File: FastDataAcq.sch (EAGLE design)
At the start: 225 parts, among them J1 MICRO-FIT_3.0_2POS_RA_SMD, J2 USB_MICROAB_SMT, U1 ADC08D500, U10 TMP421, U11 DAC101C081, U12 ADCMP553BRMZ, U13 XCFXXS04, U14 FT230XQ, U2 XC6SLX9-3TQG144C, U3 LTC2955-1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

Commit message: Minor
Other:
- note added: "1"
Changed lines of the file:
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@@
 <text x="239.522" y="157.48" size="1.778" layer="96">Green</text>
 <text x="249.682" y="157.48" size="1.778" layer="96">Red</text>
+<text x="419.1" y="7.62" size="1.778" layer="91">1</text>
 </plain>
 <instances>

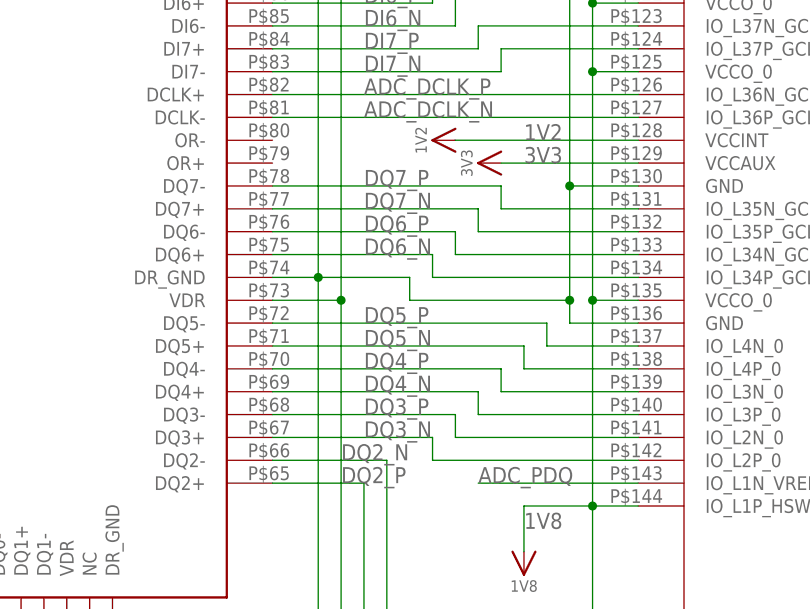
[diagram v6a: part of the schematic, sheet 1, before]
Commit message: Minor fixes
Changed some signals names.
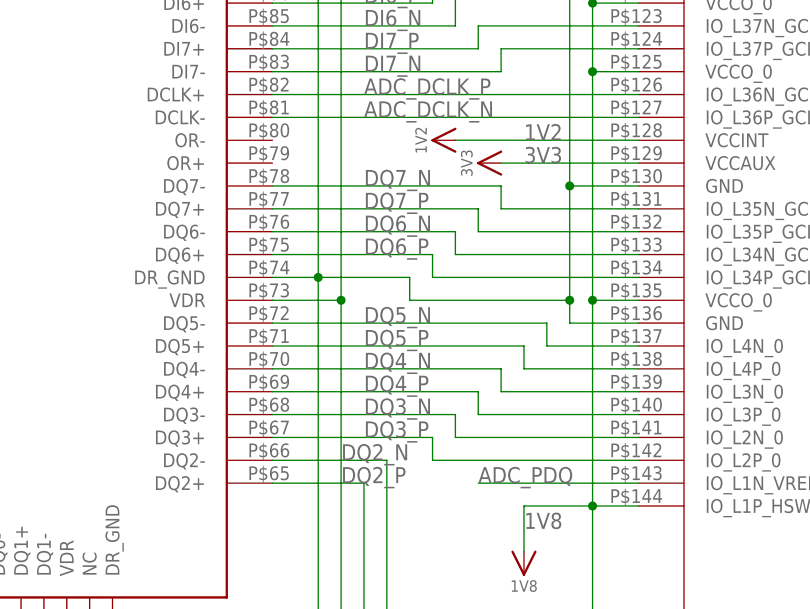
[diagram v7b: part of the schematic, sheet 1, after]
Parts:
- R39: value 50 -> 49.9
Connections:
- net DQ3_N: now also U1G$1.DQ3-, U2.IO_L2N_0; no longer U1G$1.DQ3+, U2.IO_L2P_0
- net DQ3_P: now also U1G$1.DQ3+, U2.IO_L2P_0; no longer U1G$1.DQ3-, U2.IO_L2N_0
- net DQ4_N: now also U1G$1.DQ4-, U2.IO_L3N_0; no longer U1G$1.DQ4+, U2.IO_L3P_0
- net DQ4_P: now also U1G$1.DQ4+, U2.IO_L3P_0; no longer U1G$1.DQ4-, U2.IO_L3N_0
- net DQ5_N: now also U1G$1.DQ5-, U2.IO_L4N_0; no longer U1G$1.DQ5+, U2.IO_L4P_0
- net DQ5_P: now also U1G$1.DQ5+, U2.IO_L4P_0; no longer U1G$1.DQ5-, U2.IO_L4N_0
- net DQ6_N: now also U1G$1.DQ6-, U2.IO_L34N_GCLK18_0; no longer U1G$1.DQ6+, U2.IO_L34P_GCLK19_0
- net DQ6_P: now also U1G$1.DQ6+, U2.IO_L34P_GCLK19_0; no longer U1G$1.DQ6-, U2.IO_L34N_GCLK18_0
- net DQ7_N: now also U1G$1.DQ7-, U2.IO_L35N_GCLK16_0; no longer U1G$1.DQ7+, U2.IO_L35P_GCLK17_0
- net DQ7_P: now also U1G$1.DQ7+, U2.IO_L35P_GCLK17_0; no longer U1G$1.DQ7-, U2.IO_L35N_GCLK16_0
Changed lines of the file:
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@@
 <attribute name="SUPPLIER" value="DIGIKEY"/>
 </part>
-<part name="R39" library="rcl" deviceset="R-US_" device="R0201" value="50">
+<part name="R39" library="rcl" deviceset="R-US_" device="R0201" value="49.9">
 <attribute name="MANPARTNUMBER" value="RC0603F49R9C"/>
 <attribute name="MANUFACTURER" value="Samsung Electro-Mechanics America, Inc"/>
@@
 </segment>
 </net>
-<net name="DQ7_P" class="3">
+<net name="DQ7_N" class="3">
 <segment>
 <pinref part="U1" gate="G$1" pin="DQ7-"/>
@@
 </segment>
 </net>
-<net name="DQ7_N" class="3">
-<segment>
-<pinref part="U1" gate="G$1" pin="DQ7+"/>
-<wire x1="185.42" y1="137.16" x2="208.28" y2="137.16" width="0.1524" layer="91"/>
-<wire x1="208.28" y1="137.16" x2="208.28" y2="134.62" width="0.1524" layer="91"/>
-<pinref part="U2" gate="G$1" pin="IO_L35P_GCLK17_0"/>
-<wire x1="208.28" y1="134.62" x2="226.06" y2="134.62" width="0.1524" layer="91"/>
-<label x="195.58" y="137.16" size="1.778" layer="95"/>
-</segment>
-</net>
-<net name="DQ6_P" class="3">
+<net name="DQ6_N" class="3">
 <segment>
 <pinref part="U1" gate="G$1" pin="DQ6-"/>
@@
 </segment>
 </net>
-<net name="DQ6_N" class="3">
-<segment>
-<pinref part="U1" gate="G$1" pin="DQ6+"/>
-<wire x1="185.42" y1="132.08" x2="203.2" y2="132.08" width="0.1524" layer="91"/>
-<wire x1="203.2" y1="132.08" x2="203.2" y2="129.54" width="0.1524" layer="91"/>
-<pinref part="U2" gate="G$1" pin="IO_L34P_GCLK19_0"/>
-<wire x1="203.2" y1="129.54" x2="226.06" y2="129.54" width="0.1524" layer="91"/>
-<label x="195.58" y="132.08" size="1.778" layer="95"/>
-</segment>
-</net>
-<net name="DQ5_P" class="3">
+<net name="DQ5_N" class="3">
 <segment>
 <pinref part="U1" gate="G$1" pin="DQ5-"/>
@@
 </segment>
 </net>
-<net name="DQ5_N" class="3">
-<segment>
-<pinref part="U2" gate="G$1" pin="IO_L4P_0"/>
-<wire x1="226.06" y1="119.38" x2="213.36" y2="119.38" width="0.1524" layer="91"/>
-<wire x1="213.36" y1="119.38" x2="213.36" y2="121.92" width="0.1524" layer="91"/>
-<pinref part="U1" gate="G$1" pin="DQ5+"/>
-<wire x1="213.36" y1="121.92" x2="185.42" y2="121.92" width="0.1524" layer="91"/>
-<label x="195.58" y="121.92" size="1.778" layer="95"/>
-</segment>
-</net>
-<net name="DQ4_P" class="3">
+<net name="DQ4_N" class="3">
 <segment>
 <pinref part="U1" gate="G$1" pin="DQ4-"/>
@@
 </segment>
 </net>
-<net name="DQ4_N" class="3">
-<segment>
-<pinref part="U2" gate="G$1" pin="IO_L3P_0"/>
-<wire x1="226.06" y1="114.3" x2="208.28" y2="114.3" width="0.1524" layer="91"/>
-<wire x1="208.28" y1="114.3" x2="208.28" y2="116.84" width="0.1524" layer="91"/>
-<pinref part="U1" gate="G$1" pin="DQ4+"/>
-<wire x1="208.28" y1="116.84" x2="185.42" y2="116.84" width="0.1524" layer="91"/>
-<label x="195.58" y="116.84" size="1.778" layer="95"/>
-</segment>
-</net>
-<net name="DQ3_P" class="3">
+<net name="DQ3_N" class="3">
 <segment>
 <pinref part="U1" gate="G$1" pin="DQ3-"/>
@@
 <wire x1="205.74" y1="111.76" x2="226.06" y2="111.76" width="0.1524" layer="91"/>
 <label x="195.58" y="114.3" size="1.778" layer="95"/>
-</segment>
-</net>
-<net name="DQ3_N" class="3">
-<segment>
-<pinref part="U1" gate="G$1" pin="DQ3+"/>
-<wire x1="185.42" y1="111.76" x2="203.2" y2="111.76" width="0.1524" layer="91"/>
-<wire x1="203.2" y1="111.76" x2="203.2" y2="109.22" width="0.1524" layer="91"/>
-<pinref part="U2" gate="G$1" pin="IO_L2P_0"/>
-<wire x1="203.2" y1="109.22" x2="226.06" y2="109.22" width="0.1524" layer="91"/>
-<label x="195.58" y="111.76" size="1.778" layer="95"/>
 </segment>
 </net>
@@
 </segment>
 </net>
+<net name="DQ7_P" class="3">
+<segment>
+<pinref part="U1" gate="G$1" pin="DQ7+"/>
+<wire x1="185.42" y1="137.16" x2="208.28" y2="137.16" width="0.1524" layer="91"/>
+<wire x1="208.28" y1="137.16" x2="208.28" y2="134.62" width="0.1524" layer="91"/>
+<pinref part="U2" gate="G$1" pin="IO_L35P_GCLK17_0"/>
+<wire x1="208.28" y1="134.62" x2="226.06" y2="134.62" width="0.1524" layer="91"/>
+<label x="195.58" y="137.16" size="1.778" layer="95"/>
+</segment>
+</net>
+<net name="DQ6_P" class="3">
+<segment>
+<pinref part="U1" gate="G$1" pin="DQ6+"/>
+<wire x1="185.42" y1="132.08" x2="203.2" y2="132.08" width="0.1524" layer="91"/>
+<wire x1="203.2" y1="132.08" x2="203.2" y2="129.54" width="0.1524" layer="91"/>
+<pinref part="U2" gate="G$1" pin="IO_L34P_GCLK19_0"/>
+<wire x1="203.2" y1="129.54" x2="226.06" y2="129.54" width="0.1524" layer="91"/>
+<label x="195.58" y="132.08" size="1.778" layer="95"/>
+</segment>
+</net>
+<net name="DQ5_P" class="3">
+<segment>
+<pinref part="U2" gate="G$1" pin="IO_L4P_0"/>
+<wire x1="226.06" y1="119.38" x2="213.36" y2="119.38" width="0.1524" layer="91"/>
+<wire x1="213.36" y1="119.38" x2="213.36" y2="121.92" width="0.1524" layer="91"/>
+<pinref part="U1" gate="G$1" pin="DQ5+"/>
+<wire x1="213.36" y1="121.92" x2="185.42" y2="121.92" width="0.1524" layer="91"/>
+<label x="195.58" y="121.92" size="1.778" layer="95"/>
+</segment>
+</net>
+<net name="DQ4_P" class="3">
+<segment>
+<pinref part="U2" gate="G$1" pin="IO_L3P_0"/>
+<wire x1="226.06" y1="114.3" x2="208.28" y2="114.3" width="0.1524" layer="91"/>
+<wire x1="208.28" y1="114.3" x2="208.28" y2="116.84" width="0.1524" layer="91"/>
+<pinref part="U1" gate="G$1" pin="DQ4+"/>
+<wire x1="208.28" y1="116.84" x2="185.42" y2="116.84" width="0.1524" layer="91"/>
+<label x="195.58" y="116.84" size="1.778" layer="95"/>
+</segment>
+</net>
+<net name="DQ3_P" class="3">
+<segment>
+<pinref part="U1" gate="G$1" pin="DQ3+"/>
+<wire x1="185.42" y1="111.76" x2="203.2" y2="111.76" width="0.1524" layer="91"/>
+<wire x1="203.2" y1="111.76" x2="203.2" y2="109.22" width="0.1524" layer="91"/>
+<pinref part="U2" gate="G$1" pin="IO_L2P_0"/>
+<wire x1="203.2" y1="109.22" x2="226.06" y2="109.22" width="0.1524" layer="91"/>
+<label x="195.58" y="111.76" size="1.778" layer="95"/>
+</segment>
+</net>
